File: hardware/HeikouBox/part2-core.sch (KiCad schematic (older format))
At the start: 21 parts, among them J201 Conn_02x05_Odd_Even, J202 Conn_02x08_Odd_Even, U201 HeikouBox-Core, U202 74HCU04, Y201 14.31818MHz, Y202 28.37516MHz

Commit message: More tidy up, move vias
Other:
- moved on the sheet: C202, C203, C204, C205, R201, R202, R203, R204, U201A, U201B, U201C, U201D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

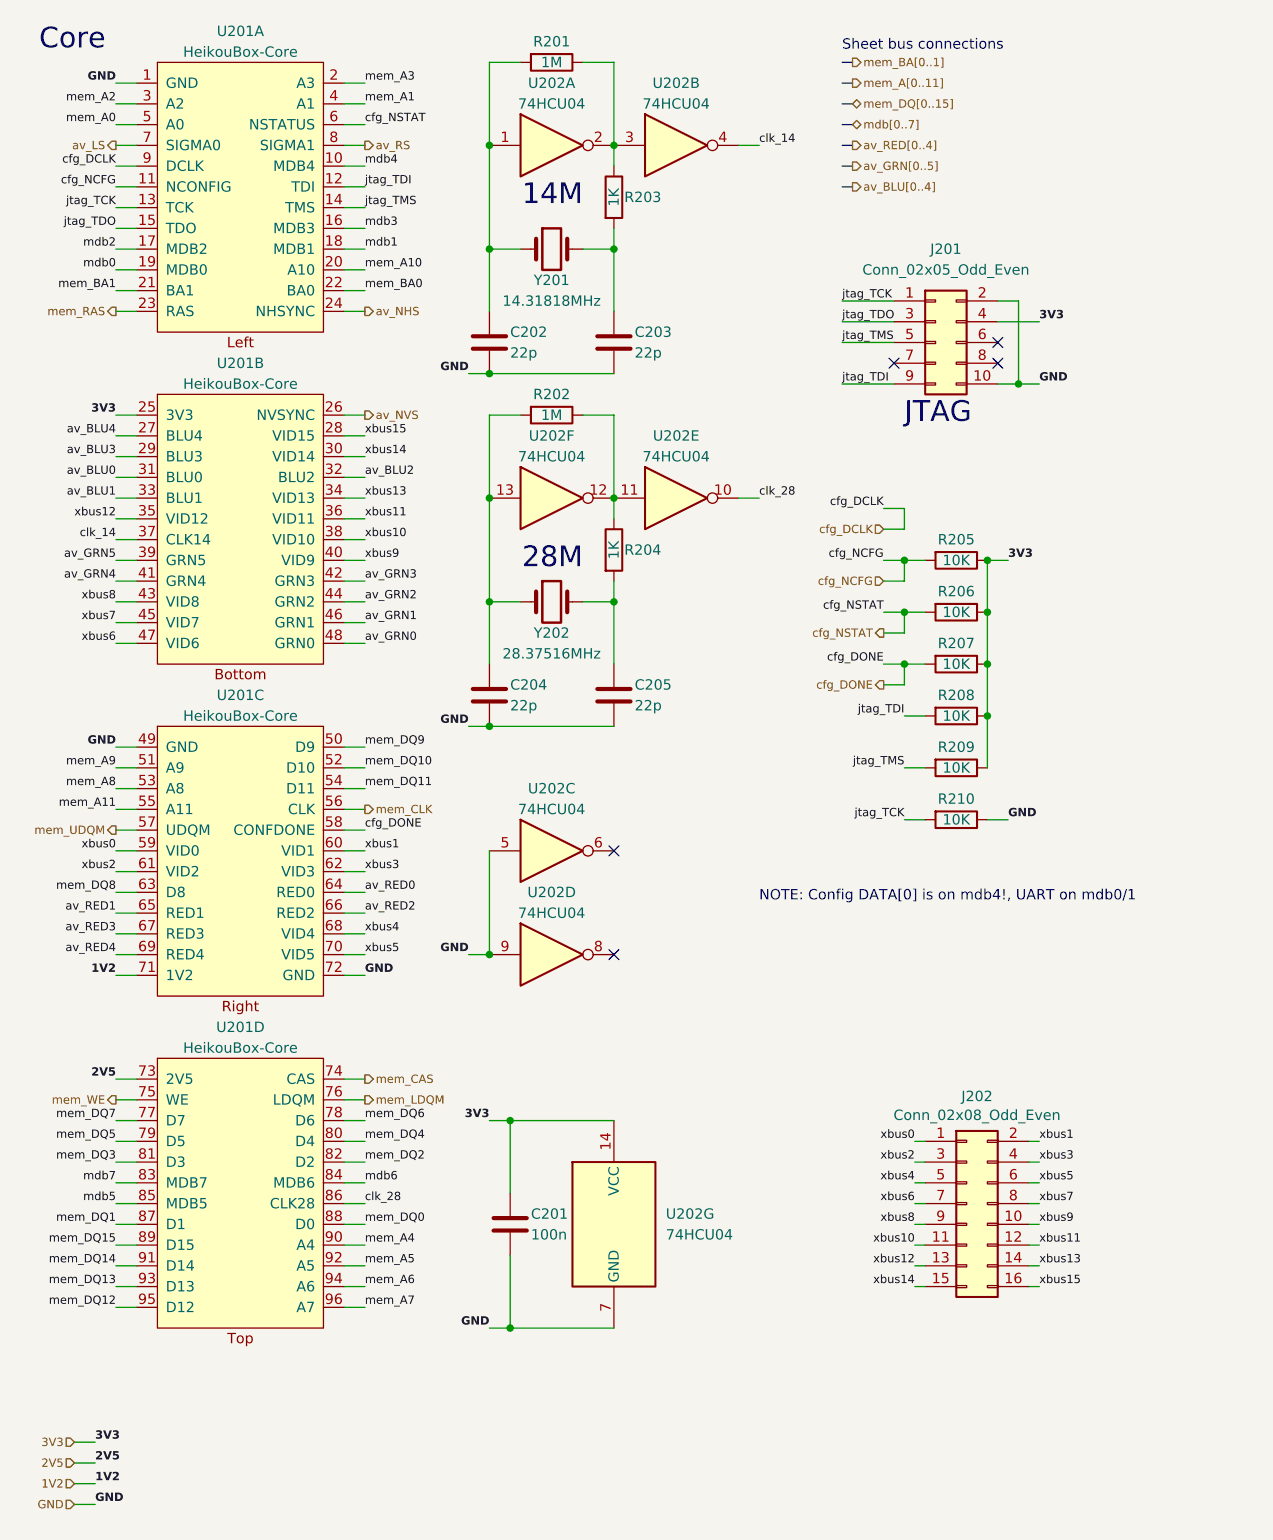
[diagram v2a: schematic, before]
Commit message: Shrink VGA ladders to make space for xbus redo
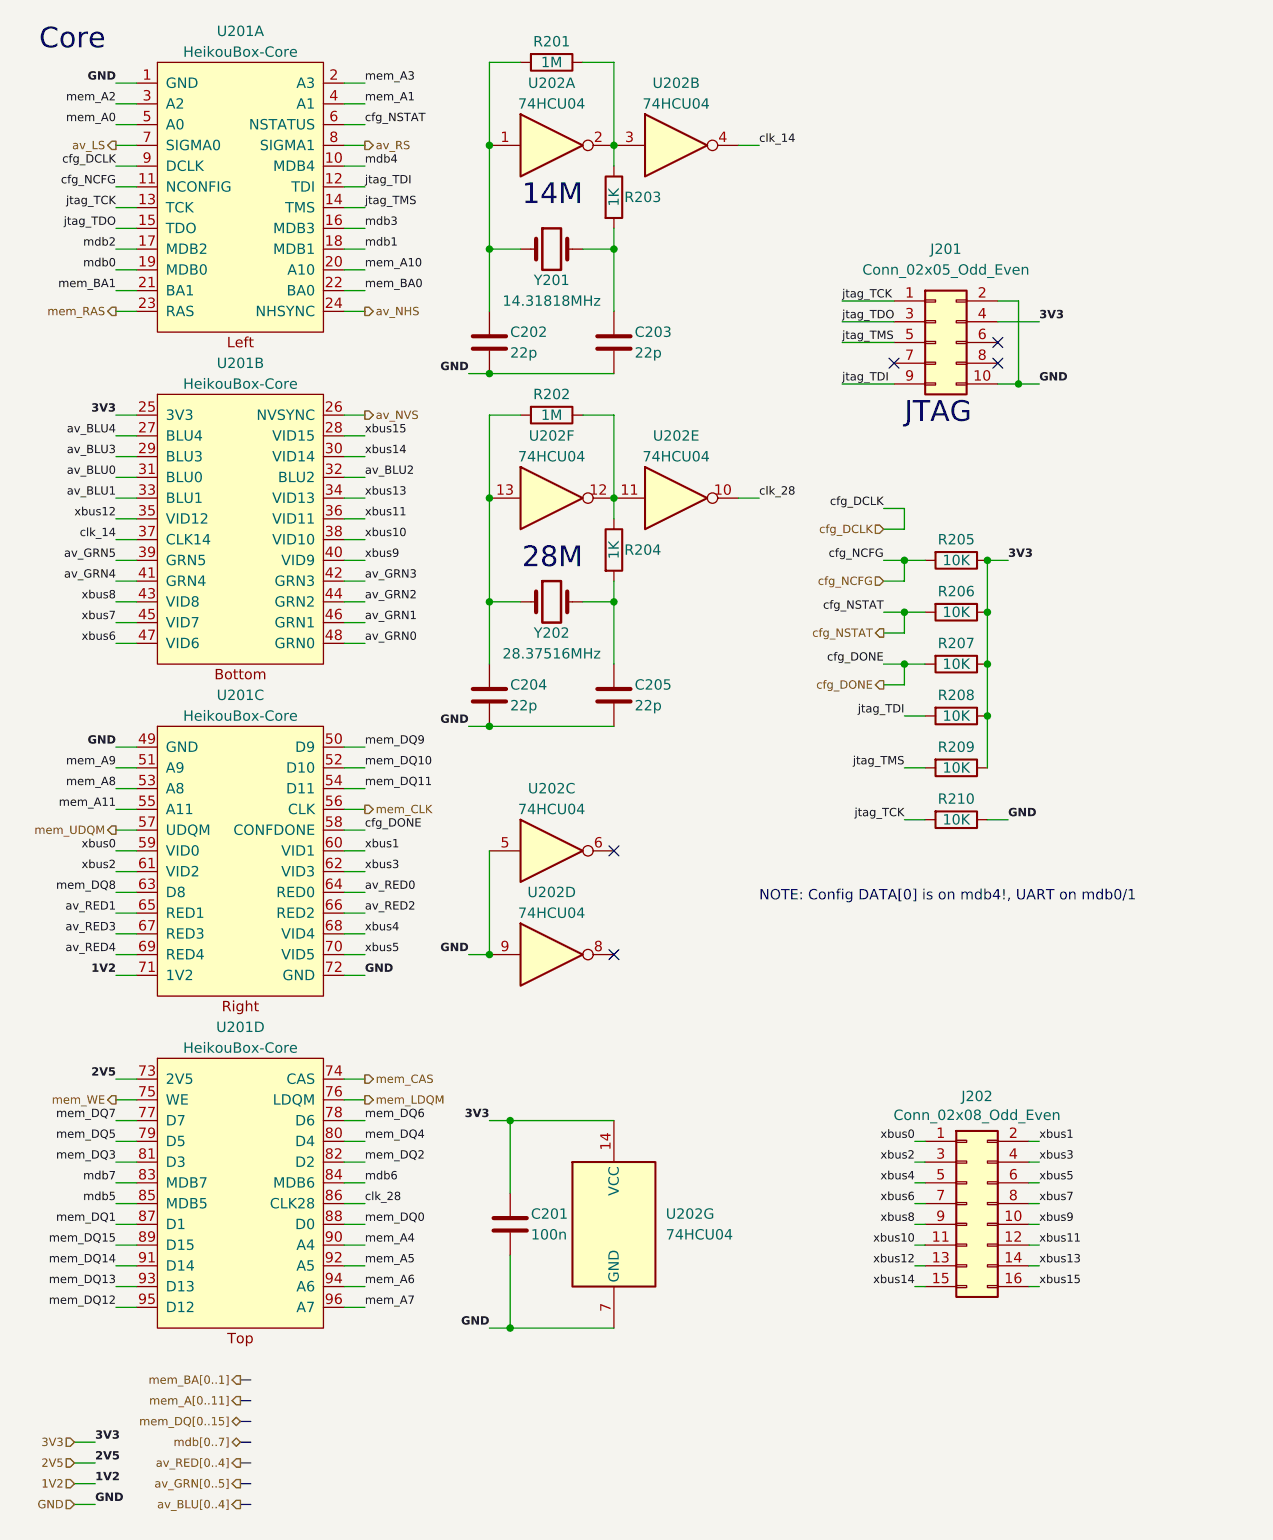
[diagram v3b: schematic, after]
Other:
- note removed: "Sheet bus connections"
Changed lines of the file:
@@
 Text Label 4700 4350 2    40   ~ 0
 jtag_TCK
-Text HLabel 700  7350 0    40   Input ~ 0
-3V3
 Wire Wire Line
 	2700 4500 2700 5000
-Wire Wire Line
-	700  7650 800  7650
-Text HLabel 700  7650 0    40   Input ~ 0
-GND
 Wire Wire Line
 	3300 6800 2800 6800
@@
 NOTE: Config DATA[0] is on mdb4!, UART on mdb0/1
 Wire Bus Line
-	4450 700  4400 700
-Text Notes 4400 650  0    50   ~ 0
-Sheet bus connections
-Text HLabel 4450 700  2    40   Output ~ 0
+	1550 7050 1500 7050
+Text HLabel 1500 7050 0    40   Output ~ 0
 mem_BA[0..1]
-Text HLabel 4450 800  2    40   Output ~ 0
+Text HLabel 1500 7150 0    40   Output ~ 0
 mem_A[0..11]
 Wire Bus Line
-	4450 800  4400 800
-Text HLabel 4450 900  2    40   BiDi ~ 0
+	1550 7150 1500 7150
+Text HLabel 1500 7250 0    40   BiDi ~ 0
 mem_DQ[0..15]
 Wire Bus Line
-	4450 900  4400 900
-Text HLabel 4450 1000 2    40   BiDi ~ 0
+	1550 7250 1500 7250
+Text HLabel 1500 7350 0    40   BiDi ~ 0
 mdb[0..7]
 Wire Bus Line
-	4450 1000 4400 1000
-Text HLabel 4450 1100 2    40   Output ~ 0
+	1550 7350 1500 7350
+Text HLabel 1500 7450 0    40   Output ~ 0
 av_RED[0..4]
-Text HLabel 4450 1200 2    40   Output ~ 0
+Text HLabel 1500 7550 0    40   Output ~ 0
 av_GRN[0..5]
-Text HLabel 4450 1300 2    40   Output ~ 0
+Text HLabel 1500 7650 0    40   Output ~ 0
 av_BLU[0..4]
 Wire Bus Line
-	4450 1100 4400 1100
+	1550 7450 1500 7450
 Wire Bus Line
-	4450 1200 4400 1200
+	1550 7550 1500 7550
 Wire Bus Line
-	4450 1300 4400 1300
+	1550 7650 1500 7650
 Wire Wire Line
 	2700 3900 3300 3900
@@
 	2800 5800 2700 5800
 Connection ~ 2800 5800
-Text Label 800  7350 0    40   ~ 8
-3V3
-Wire Wire Line
-	700  7350 800  7350
 Text Label 2700 5800 2    40   ~ 8
 3V3
@@
 GND
 Connection ~ 2800 6800
-Text Label 800  7650 0    40   ~ 8
-GND
 Wire Wire Line
 	2700 5000 2600 5000
@@
 Wire Wire Line
 	5150 1950 5350 1950
-Text HLabel 700  7450 0    40   Input ~ 0
-2V5
-Text Label 800  7450 0    40   ~ 8
-2V5
-Wire Wire Line
-	700  7450 800  7450
-Text HLabel 700  7550 0    40   Input ~ 0
-1V2
-Text Label 800  7550 0    40   ~ 8
-1V2
-Wire Wire Line
-	700  7550 800  7550
 Text Label 4600 3350 2    40   ~ 0
 cfg_NSTAT
@@
 	1    0    0    -1
 $EndComp
+Wire Wire Line
+	700  7550 800  7550
+Text Label 800  7550 0    40   ~ 8
+1V2
+Text HLabel 700  7550 0    40   Input ~ 0
+1V2
+Wire Wire Line
+	700  7450 800  7450
+Text Label 800  7450 0    40   ~ 8
+2V5
+Text HLabel 700  7450 0    40   Input ~ 0
+2V5
+Text Label 800  7650 0    40   ~ 8
+GND
+Wire Wire Line
+	700  7350 800  7350
+Text Label 800  7350 0    40   ~ 8
+3V3
+Text HLabel 700  7650 0    40   Input ~ 0
+GND
+Wire Wire Line
+	700  7650 800  7650
+Text HLabel 700  7350 0    40   Input ~ 0
+3V3
 $EndSCHEMATC
